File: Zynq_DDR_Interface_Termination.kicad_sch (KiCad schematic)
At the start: 43 parts, among them U200 XC7Z010-2CLG400I

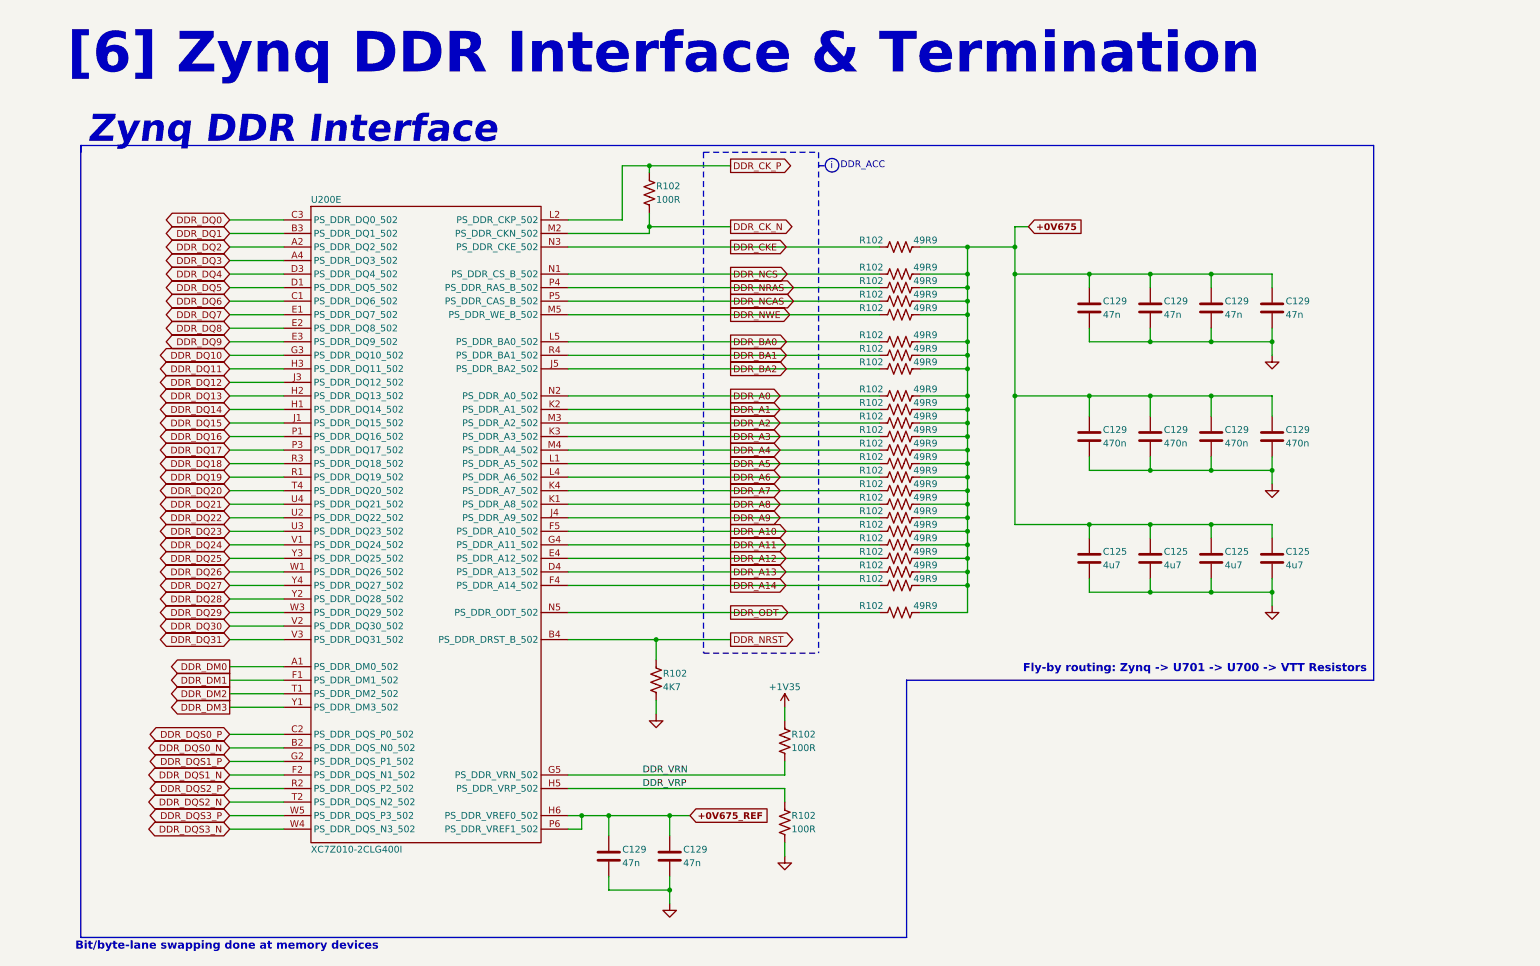
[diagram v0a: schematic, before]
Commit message: Added page '[7] 1GB DDR3L Modules'
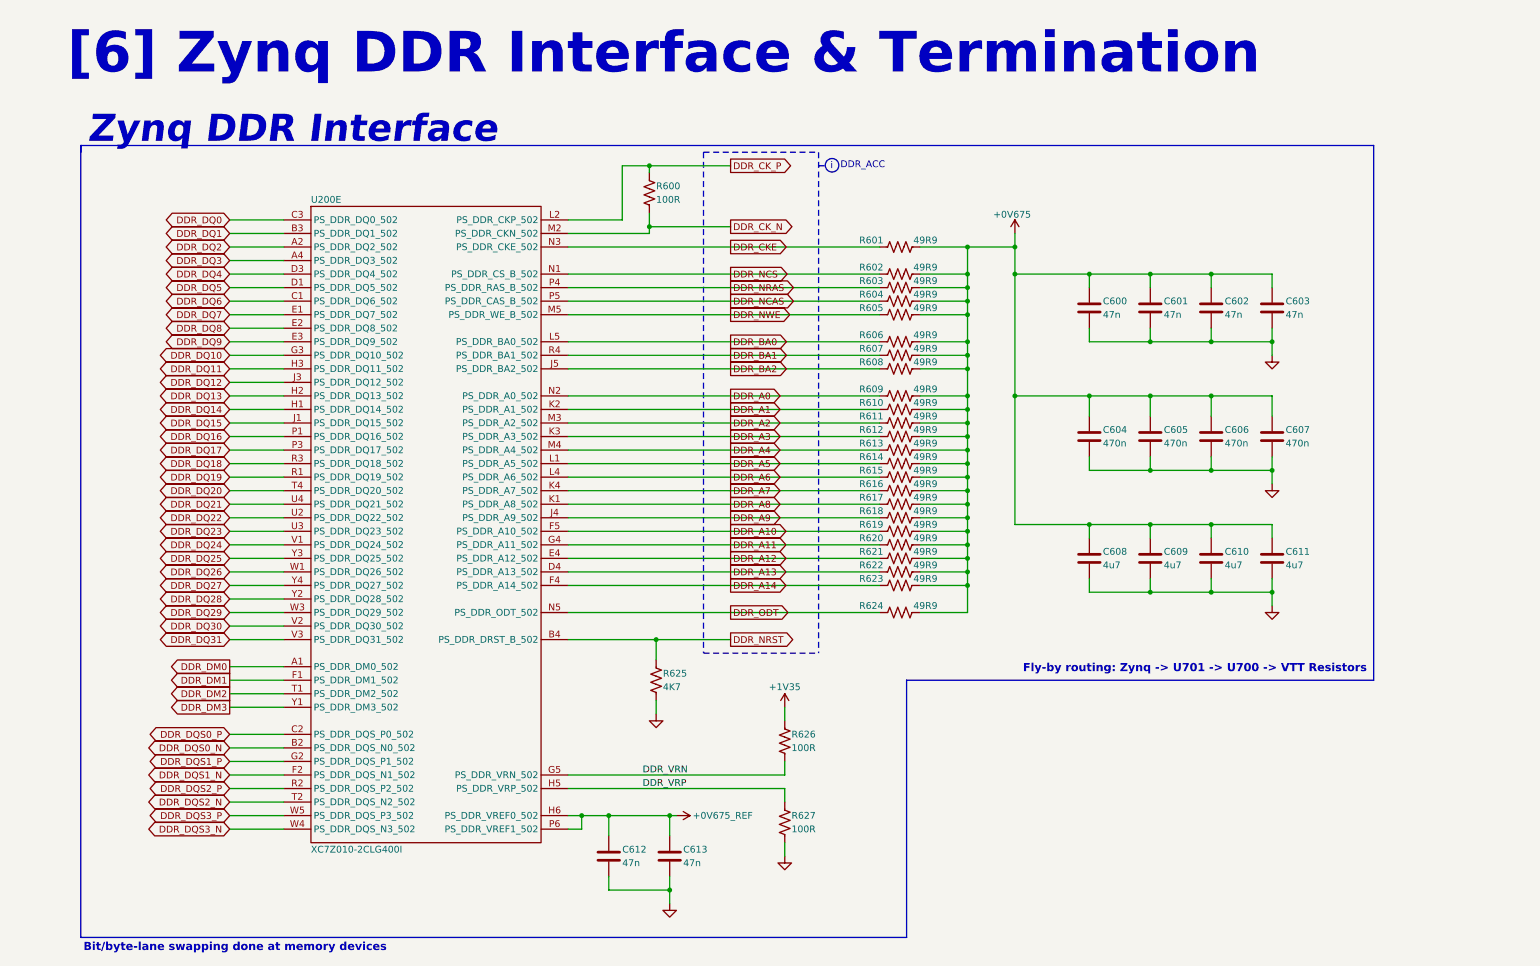
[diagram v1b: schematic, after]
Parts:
- renumbered C129 to C600, C129 to C601, C129 to C602, C129 to C603, C129 to C604, C129 to C605, C129 to C606, C129 to C607, C125 to C608, C125 to C609, C125 to C610, C125 to C611, C129 to C612, C129 to C613, R102 to R600, R102 to R601, R102 to R602, R102 to R603, R102 to R604, R102 to R605, R102 to R606, R102 to R607, R102 to R608, R102 to R609, R102 to R610, R102 to R611, R102 to R612, R102 to R613, R102 to R614, R102 to R615, R102 to R616, R102 to R617, R102 to R618, R102 to R619, R102 to R620, R102 to R621, R102 to R622, R102 to R623, R102 to R624, R102 to R625, R102 to R626, R102 to R627
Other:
- company: (none) -> Designed By: Dylan Gutierrez

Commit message: Finished first pass of schematic, needs netclass assignments and double check
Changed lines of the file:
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@@
 		(dnp no)
 		(property "Reference" "U200"
-			(at 59.69 50.8 0)
+			(at 59.944 50.8 0)
 			(effects
 				(font
@@
 		)
 		(property "Value" "XC7Z010-2CLG400I"
-			(at 59.69 172.72 0)
+			(at 83.566 173.228 0)
 			(effects
 				(font
@@
 		)
 		(instances
-			(project "ZeBra-X"
+			(project ""
+				(path "/ec71d28a-654e-4dfb-b412-dd09b7b3e4b8/369d50d7-e508-4bcb-a2d0-a2c7d0c5b870"
+					(reference "U200")
+					(unit 5)
+				)
 				(path "/ec71d28a-654e-4dfb-b412-dd09b7b3e4b8/6654cd68-a29c-475c-8e14-c9bab4900934"
 					(reference "U200")
